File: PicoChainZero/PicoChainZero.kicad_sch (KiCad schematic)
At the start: 41 parts, among them J1 RJ45, J2 RJ45, J3 Raspberry Pi, J4 USB_C_Receptacle_USB2.0_14P, J5 +12V In, J6 +24V In, J7 Conn_01x02_Pin, J8 Conn_01x02_Pin, U1 LM78M05, U2 FT232RL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

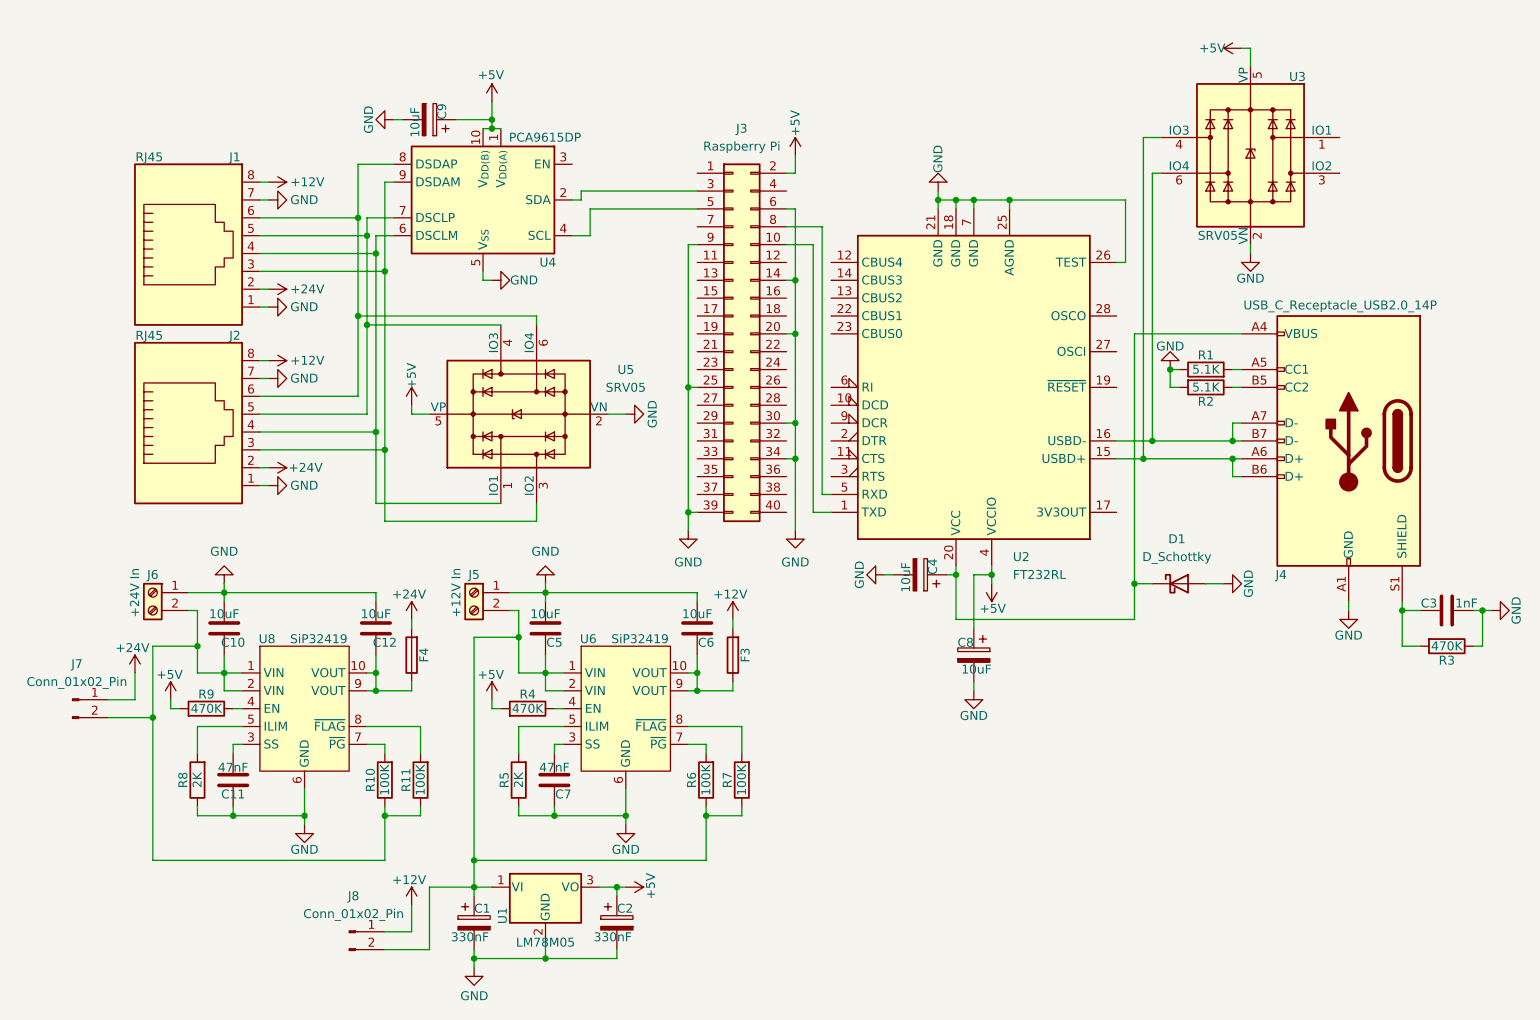
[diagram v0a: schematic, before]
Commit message: Adjusted schematics
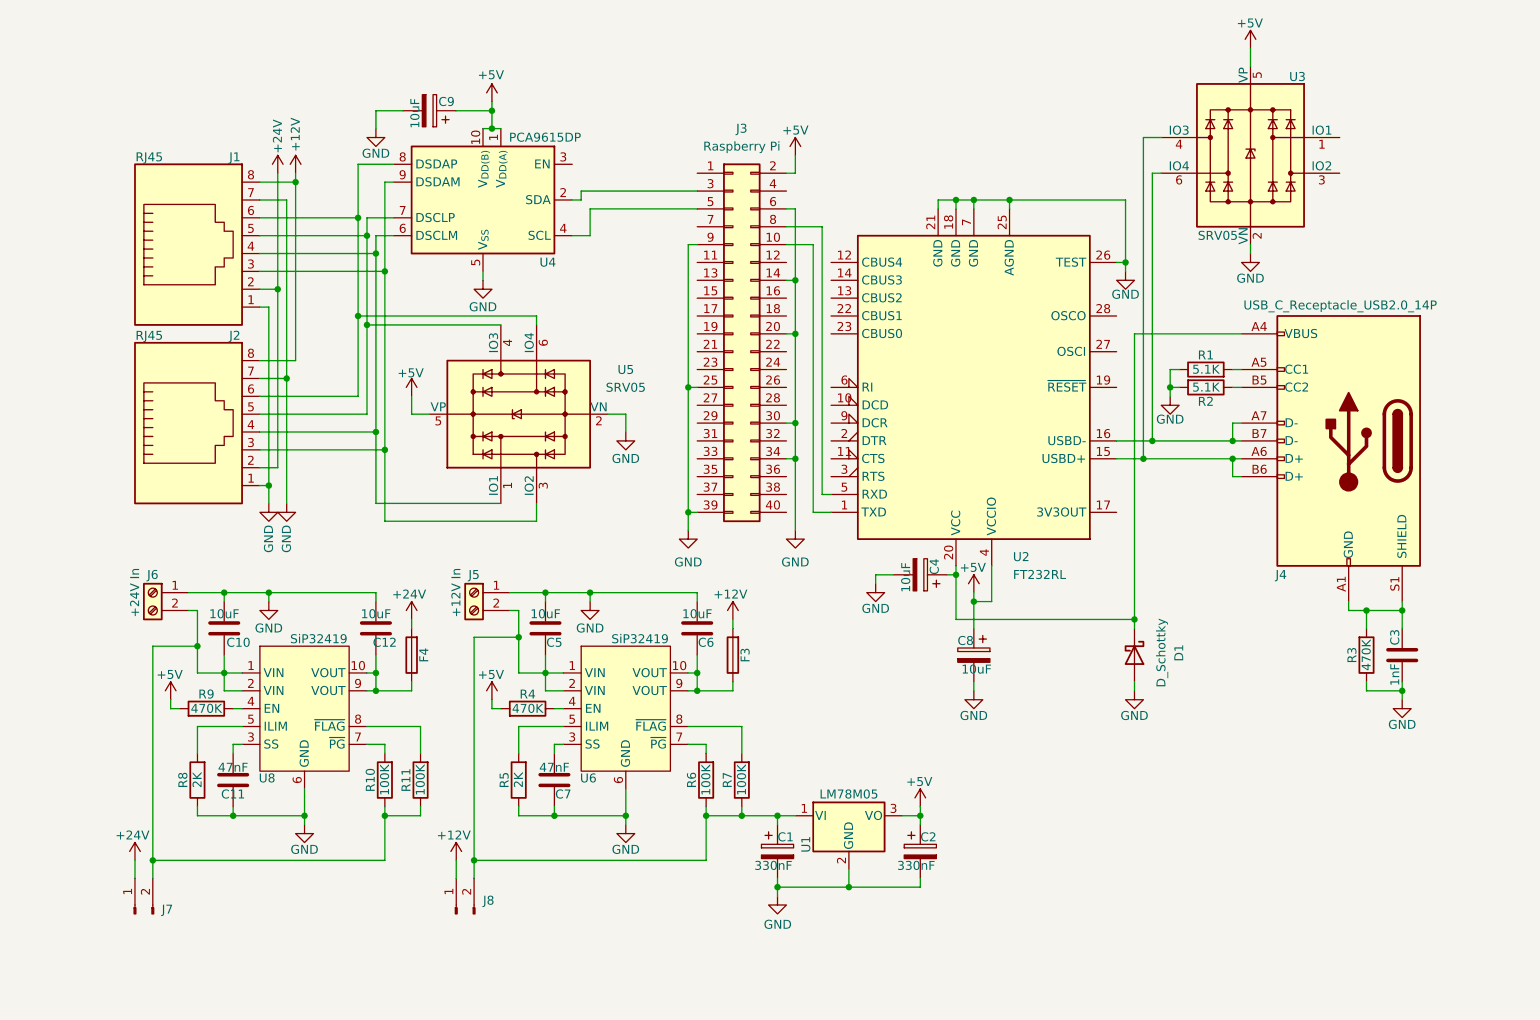
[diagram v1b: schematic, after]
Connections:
- net GND: no longer J4.A1 (GND), J4.A12 (GND), J4.B1 (GND), J4.B12 (GND)
- net at C3.1, J4.S1 (SHIELD), R3.2: now also J4.A1 (GND), J4.A12 (GND), J4.B1 (GND), J4.B12 (GND)
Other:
- moved on the sheet: C1, C2, C3, C9, D1, J7, J8, R3, U1

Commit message: Finial changes before ordering first boards.
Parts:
- removed C9: 10uF, Capacitor_Tantalum_SMD:CP_EIA-3216-18_Kemet-A, symbol Device:C_Polarized
- added C13: 10uF, Capacitor_SMD:C_0805_2012Metric, symbol Device:C
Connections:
- net +5V: now also C13.2
- net GND: now also C13.1
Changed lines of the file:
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@@
-	)
-	(symbol
-		(lib_id "Device:C_Polarized")
-		(at 97.79 41.91 270)
-		(mirror x)
-		(unit 1)
-		(exclude_from_sim no)
-		(in_bom yes)
-		(on_board yes)
-		(dnp no)
-		(property "Reference" "C9"
-			(at 99.06 40.64 90)
-			(effects
-				(font
-					(size 1.27 1.27)
-				)
-				(justify left)
-			)
-		)
-		(property "Value" "10uF"
-			(at 95.758 44.45 0)
-			(effects
-				(font
-					(size 1.27 1.27)
-				)
-				(justify left)
-			)
-		)
-		(property "Footprint" "Capacitor_Tantalum_SMD:CP_EIA-3216-18_Kemet-A"
-			(at 93.98 40.9448 0)
-			(effects
-				(font
-					(size 1.27 1.27)
-				)
-				(hide yes)
-			)
-		)
-		(property "Datasheet" "~"
-			(at 97.79 41.91 0)
-			(effects
-				(font
-					(size 1.27 1.27)
-				)
-				(hide yes)
-			)
-		)
-		(property "Description" "Polarized capacitor"
-			(at 97.79 41.91 0)
-			(effects
-				(font
-					(size 1.27 1.27)
-				)
-				(hide yes)
-			)
-		)
-		(pin "1"
-		)
-		(pin "2"
-		)
-		(instances
-			(project "PicoChainZero"
-				(path "/bf05c66b-7ba7-46d1-8dac-29939cd00b00"
-					(reference "C9")
-					(unit 1)
-				)
-			)
-		)
 	)
 	(symbol
@@
 					(unit 1)
 				)
+			)
+		)
+	)
+	(symbol
+		(lib_id "Device:C")
+		(at 97.79 41.91 90)
+		(unit 1)
+		(exclude_from_sim no)
+		(in_bom yes)
+		(on_board yes)
+		(dnp no)
+		(property "Reference" "C13"
+			(at 100.838 40.64 90)
+			(effects
+				(font
+					(size 1.27 1.27)
+				)
+			)
+		)
+		(property "Value" "10uF"
+			(at 95.758 41.91 0)
+			(effects
+				(font
+					(size 1.27 1.27)
+				)
+			)
+		)
+		(property "Footprint" "Capacitor_SMD:C_0805_2012Metric"
+			(at 101.6 40.9448 0)
+			(effects
+				(font
+					(size 1.27 1.27)
+				)
+				(hide yes)
+			)
+		)
+		(property "Datasheet" "~"
+			(at 97.79 41.91 0)
+			(effects
+				(font
+					(size 1.27 1.27)
+				)
+				(hide yes)
+			)
+		)
+		(property "Description" "Unpolarized capacitor"
+			(at 97.79 41.91 0)
+			(effects
+				(font
+					(size 1.27 1.27)
+				)
+				(hide yes)
+			)
+		)
+		(pin "2"
+		)
+		(pin "1"
+		)
+		(instances
+			(project "PicoChainZero"
+				(path "/bf05c66b-7ba7-46d1-8dac-29939cd00b00"
+					(reference "C13")
+					(unit 1)
+				)
